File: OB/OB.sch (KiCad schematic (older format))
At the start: 4 parts

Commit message: Progress on wifi
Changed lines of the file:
@@
 $Descr A4 11693 8268
 encoding utf-8
-Sheet 1 3
+Sheet 1 4
 Title ""
 Date ""
@@
 $EndSheet
 $Sheet
-S 4400 1300 1500 850
+S 3650 1300 1500 850
 U 5BC231CE
 F0 "All V3s input output" 50
 F1 "io.sch" 50
+F2 "USB_D_N" B R 5150 1500 50
+F3 "USB_D_P" B R 5150 1650 50
 $EndSheet
 $Comp
@@
 	1    0    0    -1
 $EndComp
+$Sheet
+S 6600 1750 2100 2600
+U 5C7A02C5
+F0 "WIFI" 50
+F1 "WIFI.sch" 50
+$EndSheet
 $EndSCHEMATC

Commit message: wifi antenna done
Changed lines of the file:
@@
 $EndComp
 $Sheet
-S 6600 1750 2100 2600
+S 6500 1300 2100 2600
 U 5C7A02C5
 F0 "WIFI" 50
 F1 "WIFI.sch" 50
+F2 "USB_D_P" B L 6500 1650 50
+F3 "USB_D_N" B L 6500 1500 50
 $EndSheet
+Wire Wire Line
+	5150 1500 6500 1500
+Wire Wire Line
+	6500 1650 5150 1650
 $EndSCHEMATC

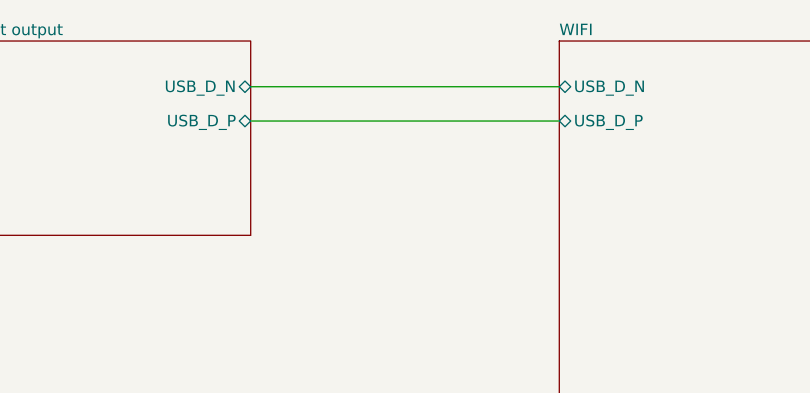
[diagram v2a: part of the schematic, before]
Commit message: +esp32picod4 +fix mounting hole position -ceramic antenna +ufl -spi flash
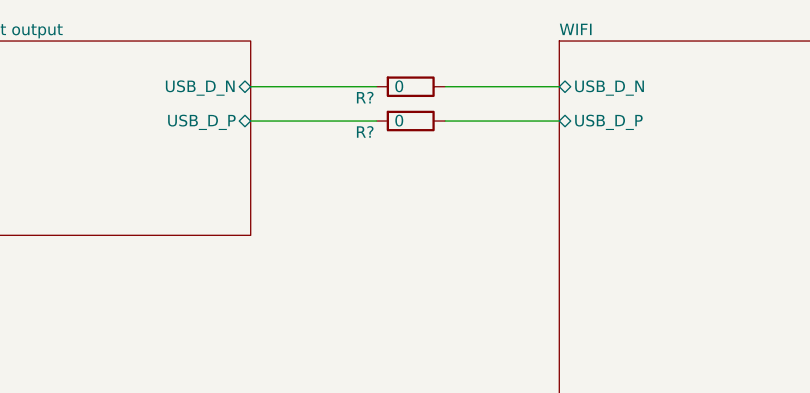
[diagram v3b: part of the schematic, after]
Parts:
- added R? (x2): 0, Resistor_SMD:R_0402_1005Metric, symbol Device:R
- MH1, MH2, MH3, MH4: footprint MountingHole:MountingHole_2.5mm_Pad_Via -> MountingHole:MountingHole_3.2mm_M3_ISO14580_Pad
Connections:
- net All V3s input output/USB_D_N: now also R?.2
- net All V3s input output/USB_D_P: now also R?.2
- new net WIFI/USB_D_N: R?.1
- new net WIFI/USB_D_P: R?.1
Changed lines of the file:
@@
 EESchema Schematic File Version 4
 LIBS:OB-cache
-EELAYER 26 0
+EELAYER 29 0
 EELAYER END
 $Descr A4 11693 8268
@@
 F 0 "MH1" H 1500 3551 50  0000 L CNN
 F 1 "MountingHole_Pad" H 1500 3460 50  0000 L CNN
-F 2 "MountingHole:MountingHole_2.5mm_Pad_Via" H 1400 3500 50  0001 C CNN
+F 2 "MountingHole:MountingHole_3.2mm_M3_ISO14580_Pad" H 1400 3500 50  0001 C CNN
 F 3 "~" H 1400 3500 50  0001 C CNN
 	1    1400 3500
@@
 F 0 "MH2" H 1500 4051 50  0000 L CNN
 F 1 "MountingHole_Pad" H 1500 3960 50  0000 L CNN
-F 2 "MountingHole:MountingHole_2.5mm_Pad_Via" H 1400 4000 50  0001 C CNN
+F 2 "MountingHole:MountingHole_3.2mm_M3_ISO14580_Pad" H 1400 4000 50  0001 C CNN
 F 3 "~" H 1400 4000 50  0001 C CNN
 	1    1400 4000
@@
 F 0 "MH3" H 1500 4501 50  0000 L CNN
 F 1 "MountingHole_Pad" H 1500 4410 50  0000 L CNN
-F 2 "MountingHole:MountingHole_2.5mm_Pad_Via" H 1400 4450 50  0001 C CNN
+F 2 "MountingHole:MountingHole_3.2mm_M3_ISO14580_Pad" H 1400 4450 50  0001 C CNN
 F 3 "~" H 1400 4450 50  0001 C CNN
 	1    1400 4450
@@
 F 0 "MH4" H 1500 4951 50  0000 L CNN
 F 1 "MountingHole_Pad" H 1500 4860 50  0000 L CNN
-F 2 "MountingHole:MountingHole_2.5mm_Pad_Via" H 1400 4900 50  0001 C CNN
+F 2 "MountingHole:MountingHole_3.2mm_M3_ISO14580_Pad" H 1400 4900 50  0001 C CNN
 F 3 "~" H 1400 4900 50  0001 C CNN
 	1    1400 4900
@@
 F3 "USB_D_N" B L 6500 1500 50
 $EndSheet
+$Comp
+L Device:R R?
+U 1 1 5CA6D3D1
+P 5850 1500
+AR Path="/5C7A02C5/5CA6D3D1" Ref="R?"  Part="1"
+AR Path="/5CA6D3D1" Ref="R?"  Part="1"
+F 0 "R?" V 5900 1300 50  0000 C CNN
+F 1 "0" V 5850 1450 50  0000 C CNN
+F 2 "Resistor_SMD:R_0402_1005Metric" V 5780 1500 50  0001 C CNN
+F 3 "~" H 5850 1500 50  0001 C CNN
+	1    5850 1500
+	0    1    1    0
+$EndComp
+$Comp
+L Device:R R?
+U 1 1 5CA6D3D8
+P 5850 1650
+AR Path="/5C7A02C5/5CA6D3D8" Ref="R?"  Part="1"
+AR Path="/5CA6D3D8" Ref="R?"  Part="1"
+F 0 "R?" V 5900 1450 50  0000 C CNN
+F 1 "0" V 5850 1600 50  0000 C CNN
+F 2 "Resistor_SMD:R_0402_1005Metric" V 5780 1650 50  0001 C CNN
+F 3 "~" H 5850 1650 50  0001 C CNN
+	1    5850 1650
+	0    1    1    0
+$EndComp
 Wire Wire Line
-	5150 1500 6500 1500
+	6000 1500 6500 1500
 Wire Wire Line
-	6500 1650 5150 1650
+	6500 1650 6000 1650
+Wire Wire Line
+	5700 1650 5150 1650
+Wire Wire Line
+	5150 1500 5700 1500
 $EndSCHEMATC
